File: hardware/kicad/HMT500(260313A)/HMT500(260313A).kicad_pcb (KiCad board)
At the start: 4 copper layers, 56.5 x 23 mm, 0 parts

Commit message: Rename project to HMT500(260313); circuit/PCB/Gerber files = HMT500(260313A)
- KiCad folder and all circuit files renamed to HMT500(260313A)*
  (top sheet, sub-sheets, symbol lib file, BOM, parts list, PDF, PCB);
  library nickname HMT500_260313A (no parentheses in lib_id)
- Title blocks carry Project No. HMT500(260313A); product HMT500(260313)
- PCB bottom silkscreen marking "HMT500(260313A)"
- export_gerbers.sh: Gerbers/drill named HMT500(260313A)-*, zip HMT500(260313A).zip
- Docs, mech drawing title block and references updated; decision #25
- Schematic review vs datasheets/KiCad library + optimization plan
  (docs/hw/schematic-review-260313A.md), awaiting approval

Co-Authored-By: Claude Opus 5.5 <noreply@anthropic.com>
Claude-Session: https://claude.ai/code/session_01JA2o8uJsqp9Vzsg4b665ev
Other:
- board text added: "HMT500(260313A)"
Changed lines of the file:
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@@
   (paper "A4")
   (title_block
-    (title "HMT500 PCB E-301 (outline & keepouts)")
+    (title "HMT500(260313A) PCB E-301 (outline & keepouts)")
     (date "2026-09-29")
     (rev "F")
@@
     (polygon (pts (xy 144.2 112.0) (xy 148.8 112.0) (xy 148.8 109.7) (xy 144.2 109.7)))
   )
-  (gr_rect (start 103.7 92.0) (end 119.3 108.0) (layer "Dwgs.User") (width 0.1) (fill none))
-  (gr_text "MEASUREMENT" (at 111.5 93.2) (layer "Dwgs.User")
+  (gr_rect (start 103.7 92.0) (end 120.3 108.0) (layer "Dwgs.User") (width 0.1) (fill none))
+  (gr_text "MEASUREMENT" (at 112.0 93.2) (layer "Dwgs.User")
     (effects (font (size 1.0 1.0) (thickness 0.150))))
-  (gr_text "J3, PCAP04, ADS1220, Cref" (at 111.5 106.8) (layer "Dwgs.User")
+  (gr_text "J3, PCAP04, ADS1220, Cref" (at 112.0 106.8) (layer "Dwgs.User")
     (effects (font (size 0.5 0.5) (thickness 0.075))))
-  (gr_rect (start 119.7 92.0) (end 135.3 108.0) (layer "Dwgs.User") (width 0.1) (fill none))
-  (gr_text "MCU + POWER" (at 127.5 93.2) (layer "Dwgs.User")
+  (gr_rect (start 120.7 92.0) (end 135.3 108.0) (layer "Dwgs.User") (width 0.1) (fill none))
+  (gr_text "MCU + POWER" (at 128.0 93.2) (layer "Dwgs.User")
     (effects (font (size 1.0 1.0) (thickness 0.150))))
-  (gr_text "STM32G0B1, eFuse, buck, LDO" (at 127.5 106.8) (layer "Dwgs.User")
+  (gr_text "STM32G0B1, eFuse, buck, LDO" (at 128.0 106.8) (layer "Dwgs.User")
     (effects (font (size 0.5 0.5) (thickness 0.075))))
   (gr_rect (start 135.7 92.0) (end 156.3 108.0) (layer "Dwgs.User") (width 0.1) (fill none))
@@
   (gr_text "J1, DAC8760x2, TPS26611, THVD2450" (at 146.0 106.8) (layer "Dwgs.User")
     (effects (font (size 0.5 0.5) (thickness 0.075))))
-  (gr_rect (start 108.0 96.5) (end 112.0 103.5) (layer "Dwgs.User") (width 0.1) (fill none))
-  (gr_text "J3 JST SH 4P SM04B-SRSS-TB (side entry <- front)" (at 110.0 104.3) (layer "Dwgs.User")
+  (gr_rect (start 116.0 96.5) (end 120.0 103.5) (layer "Dwgs.User") (width 0.1) (fill none))
+  (gr_text "J3 JST SH 4P SM04B-SRSS-TB (side entry <- front)" (at 118.0 104.3) (layer "Dwgs.User")
     (effects (font (size 0.5 0.5) (thickness 0.075))))
   (gr_rect (start 138.0 93.6) (end 144.0 106.4) (layer "Dwgs.User") (width 0.1) (fill none))
   (gr_text "J1 JST GH 8P SM08B-GHS-TB (side entry -> rear)" (at 141.0 107.2) (layer "Dwgs.User")
     (effects (font (size 0.5 0.5) (thickness 0.075))))
+  (gr_text "HMT500(260313A)" (at 44.5 0) (layer "B.SilkS")
+    (effects (font (size 1.2 1.2) (thickness 0.18)) (justify mirror)))
   (gr_text "Component height limit per side (incl. 0.5 margin):" (at 120.0 114.0) (layer "Cmts.User")
     (effects (font (size 0.8 0.8) (thickness 0.120))))

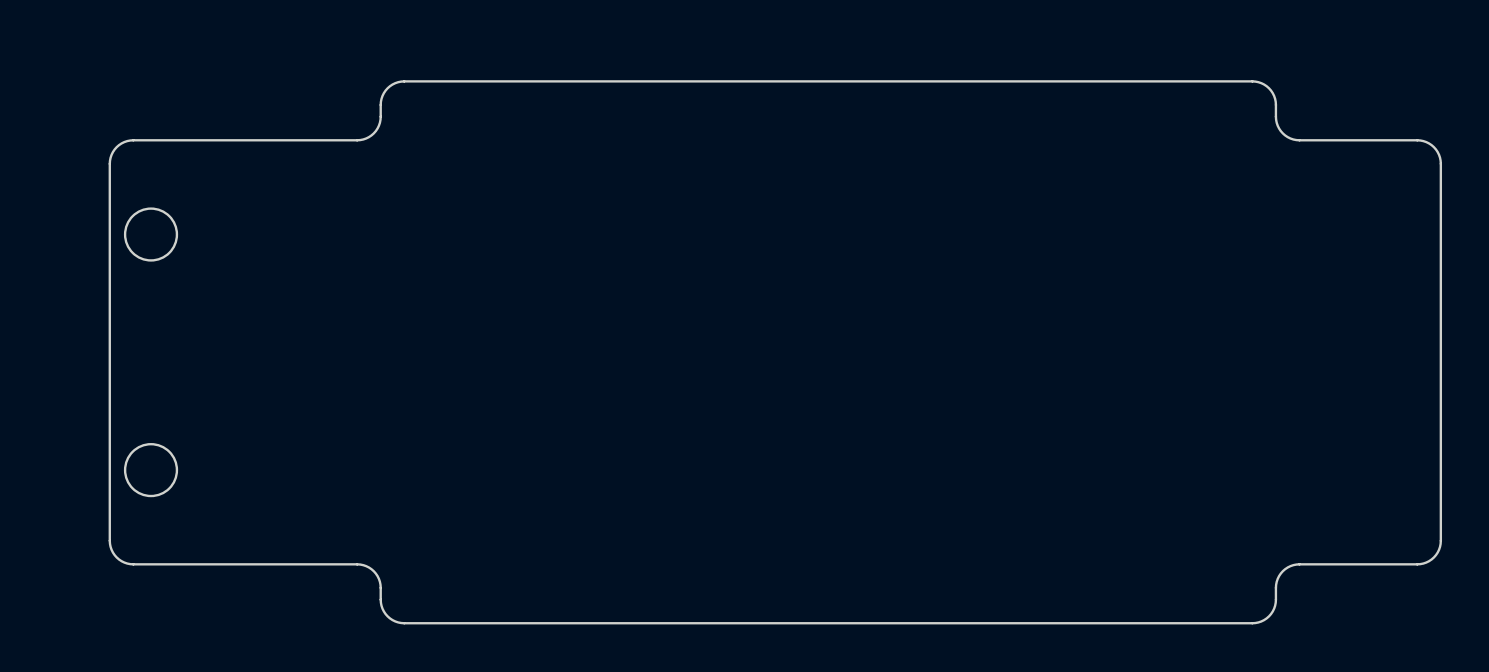
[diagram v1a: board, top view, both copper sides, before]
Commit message: PCB placement: all 84 parts placed and netted (before routing)
- place_pcb.py: fixed J3/J1/U4, hand slots for large parts, nearest-free
  search for passives; checks board edge and fillets, holder/ring keepouts,
  harness plug paths on top, height vs bore, courtyard overlap, holes
- plot_placement.py + placement.png/json (mech coords) for review and the
  assembly simulation
- Board rules for 4-layer: clearance/track 0.15, via 0.45/0.2, edge 0.3;
  .kicad_pro now merged (schematic sheet list kept)
- Custom footprints: fix local pad/line coordinates (pads were at 0,0);
  TVS3301 floating pad keeps number 9 (no symbol pin, no net)
- Placement tests; docs/hw/pcb-placement-260313A.md (J5 reach issue)

Co-Authored-By: Claude Opus 5.5 <noreply@anthropic.com>
Claude-Session: https://claude.ai/code/session_01JA2o8uJsqp9Vzsg4b665ev
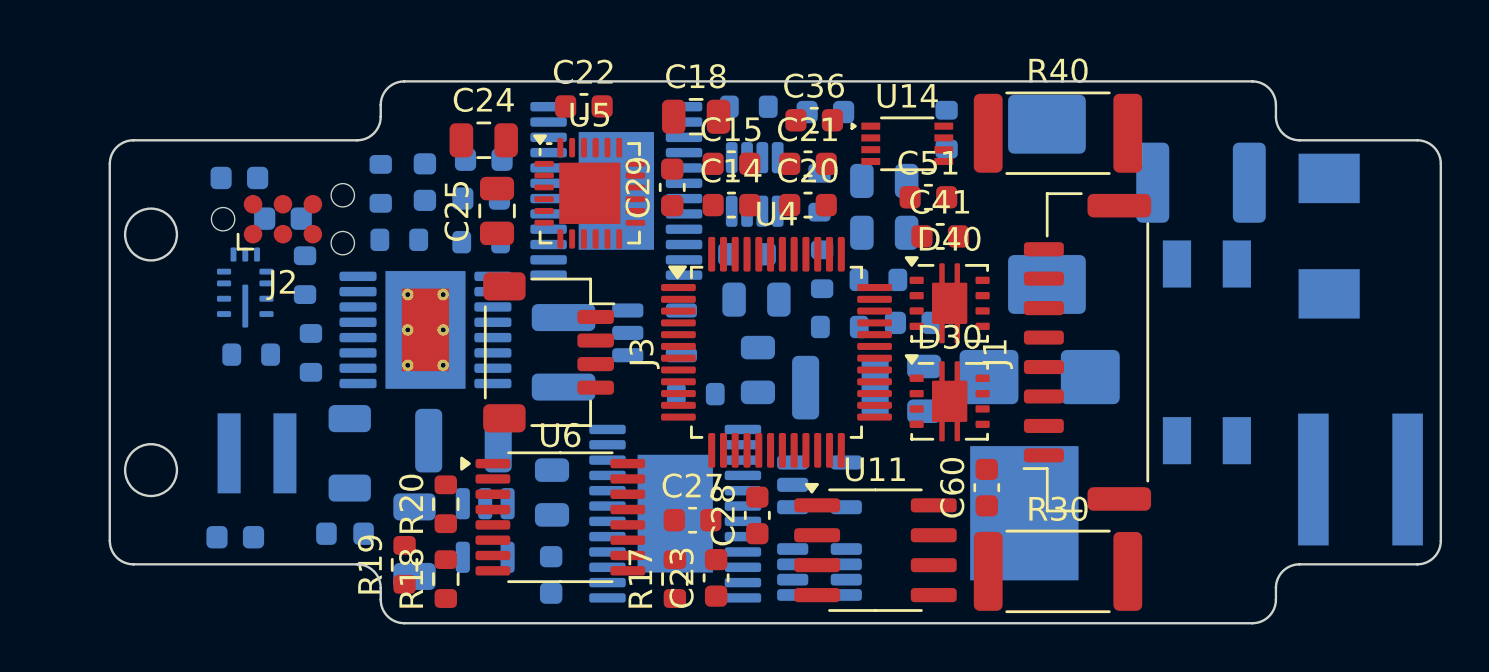
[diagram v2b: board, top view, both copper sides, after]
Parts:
- added C1: 100n 100V, Capacitor_SMD:C_0805_2012Metric, B.Cu at (134.6, 101.5)
- added C10: 22u 25V, Capacitor_SMD:C_1206_3216Metric, B.Cu at (110.2, 104.3)
- added C11: 20p C0G, Capacitor_SMD:C_0603_1608Metric, B.Cu at (105.3, 107.8)
- added C12: 1u, Capacitor_SMD:C_0603_1608Metric, B.Cu at (118.7, 109.5)
- added C13: 10u, Capacitor_SMD:C_0805_2012Metric, B.Cu at (118.8, 106.0)
- added C14: 100n, Capacitor_SMD:C_0603_1608Metric, F.Cu at (126.4, 93.8)
- added C15: 100n, Capacitor_SMD:C_0603_1608Metric, F.Cu at (126.4, 92.0)
- added C18: 4.7u, Capacitor_SMD:C_0805_2012Metric, F.Cu at (124.9, 90.0)
- added C20: 100n, Capacitor_SMD:C_0603_1608Metric, F.Cu at (129.6, 93.8)
- added C21: 100n, Capacitor_SMD:C_0603_1608Metric, F.Cu at (129.6, 92.0)
- added C22: 220p C0G 1%, Capacitor_SMD:C_0603_1608Metric, F.Cu at (120.1, 89.6)
- added C23: 100n, Capacitor_SMD:C_0603_1608Metric, F.Cu at (125.7, 109.6)
- added C24: 10u, Capacitor_SMD:C_0805_2012Metric, F.Cu at (115.9, 91.0)
- added C25: 4.7u, Capacitor_SMD:C_0805_2012Metric, F.Cu at (116.4, 94.0)
- added C27: 10n, Capacitor_SMD:C_0603_1608Metric, F.Cu at (124.7, 107.1)
- added C28: 100n, Capacitor_SMD:C_0603_1608Metric, F.Cu at (127.5, 106.9)
- added C29: 100n, Capacitor_SMD:C_0603_1608Metric, F.Cu at (123.9, 93.0)
- added C3: 4.7n 2kV Y2, Capacitor_SMD:C_1812_4532Metric, B.Cu at (146.3, 92.8)
- added C36: 100n, Capacitor_SMD:C_0603_1608Metric, F.Cu at (129.9, 90.2)
- added C4: 22n, Capacitor_SMD:C_0603_1608Metric, B.Cu at (115.8, 93.5)
- added C40: 100n, Capacitor_SMD:C_0603_1608Metric, B.Cu at (134.1, 98.8)
- added C41: 1n 100V, Capacitor_SMD:C_0603_1608Metric, F.Cu at (135.2, 95.1)
- added C42: 100n 50V, Capacitor_SMD:C_0805_2012Metric, B.Cu at (132.9, 94.9)
- added C43: 4.7u 50V, Capacitor_SMD:C_1210_3225Metric, B.Cu at (131.0, 101.5)
- added C44: 100n, Capacitor_SMD:C_0603_1608Metric, B.Cu at (113.4, 92.8)
- added C45: 100n 50V, Capacitor_SMD:C_0805_2012Metric, B.Cu at (127.5, 100.8)
- added C5: 10u 50V, Capacitor_SMD:C_1210_3225Metric, B.Cu at (119.3, 100.0)
- added C50: 100n, Capacitor_SMD:C_0603_1608Metric, B.Cu at (130.4, 89.8)
- added C51: 1n 100V, Capacitor_SMD:C_0603_1608Metric, F.Cu at (134.8, 93.4)
- added C52: 100n 50V, Capacitor_SMD:C_0805_2012Metric, B.Cu at (132.9, 92.7)
- added C54: 100n, Capacitor_SMD:C_0603_1608Metric, B.Cu at (115.9, 91.8)
- added C55: 100n 50V, Capacitor_SMD:C_0805_2012Metric, B.Cu at (127.5, 97.8)
- added C6: 22u 25V, Capacitor_SMD:C_1206_3216Metric, B.Cu at (112.9, 108.0)
- added C60: 100n, Capacitor_SMD:C_0603_1608Metric, F.Cu at (137.2, 105.7)
- added C7: 2.2u 100V, Capacitor_SMD:C_1210_3225Metric, B.Cu at (115.0, 103.8)
- added C8: 100n, Capacitor_SMD:C_0603_1608Metric, B.Cu at (107.3, 94.3)
- added C9: 1u, Capacitor_SMD:C_0603_1608Metric, B.Cu at (105.5, 92.6)
- added D1: SMDJ36CA, Diode_SMD:D_SMC, B.Cu at (139.8, 93.7)
- added D2: SMBJ33CA, Diode_SMD:D_SMB, B.Cu at (139.5, 101.0)
- added D30: TVS3301DRBR, HMT500_260313A:Texas_DRB0008A_PadFloat, F.Cu at (135.7, 102.1)
- added D40: TVS3301DRBR, HMT500_260313A:Texas_DRB0008A_PadFloat, F.Cu at (135.7, 97.9)
- added FB1: 600R@100MHz, Inductor_SMD:L_0603_1608Metric, B.Cu at (110.0, 107.7)
- added GDT1: 2035-23-SM, HMT500_260313A:GDT_Bourns_2035-xx-SM, B.Cu at (153.1, 105.4)
- added J1: SM08B-GHS-TB, Connector_JST:JST_GH_SM08B-GHS-TB_1x08-1MP_P1.25mm_Horizontal, F.Cu at (141.5, 100.0)
- added J2: TC2030-IDC-NL, Connector:Tag-Connect_TC2030-IDC-NL_2x03_P1.27mm_Vertical, F.Cu at (107.3, 94.3)
- added J3: SM04B-SRSS-TB, Connector_JST:JST_SH_SM04B-SRSS-TB_1x04-1MP_P1.00mm_Horizontal, F.Cu at (118.6, 100.0)
- added J5: S1941-46R, Connector:SpringContact_Harwin_S1941-46R, B.Cu at (139.9, 106.8)
- added L1: CMC 1mH 0.8A, Inductor_SMD:L_CommonMode_Wuerth_WE-SL2, B.Cu at (146.6, 100.0)
- added L2: 15uH, Inductor_SMD:L_Coilcraft_XAL4030-XXX, B.Cu at (106.2, 104.3)
- added R1: 4.7R 1W pulse, Resistor_SMD:R_MELF_MMB-0207, B.Cu at (151.8, 95.1)
- added R17: 1k, Resistor_SMD:R_0603_1608Metric, F.Cu at (124.0, 109.6)
- added R18: 1k, Resistor_SMD:R_0603_1608Metric, F.Cu at (114.3, 109.6)
- added R19: 4.02k 0.02% 5ppm, Resistor_SMD:R_0603_1608Metric, F.Cu at (112.5, 109.0)
- added R2: 1M, Resistor_SMD:R_0603_1608Metric, B.Cu at (135.5, 90.5)
- added R20: 1k, Resistor_SMD:R_0603_1608Metric, F.Cu at (114.3, 106.5)
- added R3: 866k 1%, Resistor_SMD:R_0603_1608Metric, B.Cu at (108.5, 100.0)
- added R30: 10R pulse, Resistor_SMD:R_2512_6332Metric, F.Cu at (140.2, 109.3)
- added R31: 10k, Resistor_SMD:R_0603_1608Metric, B.Cu at (131.0, 98.9)
- added R32: 15k 0.1% 25ppm, Resistor_SMD:R_0603_1608Metric, B.Cu at (124.9, 101.8)
- added R33: 10k, Resistor_SMD:R_0603_1608Metric, B.Cu at (127.0, 95.8)
- added R34: 10R, Resistor_SMD:R_0603_1608Metric, B.Cu at (132.6, 96.9)
- added R4: 97.6k 1%, Resistor_SMD:R_0603_1608Metric, B.Cu at (108.3, 96.7)
- added R40: 10R pulse, Resistor_SMD:R_2512_6332Metric, F.Cu at (140.2, 90.7)
- added R41: 10k, Resistor_SMD:R_0603_1608Metric, B.Cu at (130.2, 96.5)
- added R42: 15k 0.1% 25ppm, Resistor_SMD:R_0603_1608Metric, B.Cu at (127.1, 89.6)
- added R44: 10R, Resistor_SMD:R_0603_1608Metric, B.Cu at (130.1, 93.2)
- added R5: 41.2k 1%, Resistor_SMD:R_0603_1608Metric, B.Cu at (112.3, 95.2)
- added R6: 80.6k 1%, Resistor_SMD:R_0603_1608Metric, B.Cu at (115.8, 95.3)
- added R8: 100k 1%, Resistor_SMD:R_0603_1608Metric, B.Cu at (106.0, 100.1)
- added R9: 24.9k 1%, Resistor_SMD:R_0603_1608Metric, B.Cu at (111.5, 92.8)
- added U1: TPS26600PWPR, Package_SO:HTSSOP-16-1EP_4.4x5mm_P0.65mm_EP3.4x5mm_Mask2.46x2.31mm_ThermalVias, B.Cu at (113.4, 99.0)
- added U10: TPS26611DDFR, Package_TO_SOT_SMD:SOT-23-8, B.Cu at (127.4, 92.9)
- added U11: THVD2450DR, Package_SO:SOIC-8_3.9x4.9mm_P1.27mm, F.Cu at (132.5, 108.4)
- added U12: OPA197IDBVR, Package_TO_SOT_SMD:SOT-23-5, B.Cu at (130.1, 105.6)
- added U13: OPA197IDBVR, Package_TO_SOT_SMD:SOT-23-5, B.Cu at (123.1, 99.2)
- added U14: SN74LVC2G32DCUR, Package_SO:VSSOP-8_2.3x2mm_P0.5mm, F.Cu at (133.8, 91.2)
- added U2: LMR36006BRNXR, HMT500_260313A:Texas_RNX0012A_VQFN-HR-12_2x3mm, B.Cu at (105.8, 97.2)
- added U3: TPS7A2033PDBVR, Package_TO_SOT_SMD:SOT-23-5, B.Cu at (115.9, 107.6)
- added U4: STM32G0B1CCT3, Package_QFP:LQFP-48_7x7mm_P0.5mm, F.Cu at (128.3, 100.0)
- added U5: PCAP04-AQFM-24, Package_DFN_QFN:QFN-24-1EP_4x4mm_P0.5mm_EP2.6x2.6mm, F.Cu at (120.4, 93.2)
- added U6: ADS1220IPWR, Package_SO:TSSOP-16_4.4x5mm_P0.65mm, F.Cu at (119.1, 107.0)
- added U7: DAC8760IPWP, Package_SO:HTSSOP-24-1EP_4.4x7.8mm_P0.65mm_EP3.2x5mm, B.Cu at (124.0, 106.8)
- added U8: DAC8760IPWP, Package_SO:HTSSOP-24-1EP_4.4x7.8mm_P0.65mm_EP3.2x5mm, B.Cu at (121.5, 93.2)
- added U9: TPS26611DDFR, Package_TO_SOT_SMD:SOT-23-8, B.Cu at (130.1, 109.3)

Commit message: PCB placement rev 2: relax harness paths, use the freed top area
- Top harness paths: only plug body + insertion/grip space kept empty;
  under W-1 wires (z 2.2) and W-2 wires parts up to 1.0 mm allowed;
  last 2 mm before the M12 end kept empty (wires drop over the edge)
- J2 Tag-Connect (flat) moved under the W-1 wires; LDO U3, FB1, C12, C13
  moved to the freed top front area (+3V3A right at the measurement)
- eFuse U1 under the J3 plug path (its thermal-via top pad needs a
  part-free top); buck loop U2-L2-C10/C6 tightened; U14 next to MCU
- Bands stored in placement.json; plot and tests read them

Co-Authored-By: Claude Opus 5.5 <noreply@anthropic.com>
Claude-Session: https://claude.ai/code/session_01JA2o8uJsqp9Vzsg4b665ev
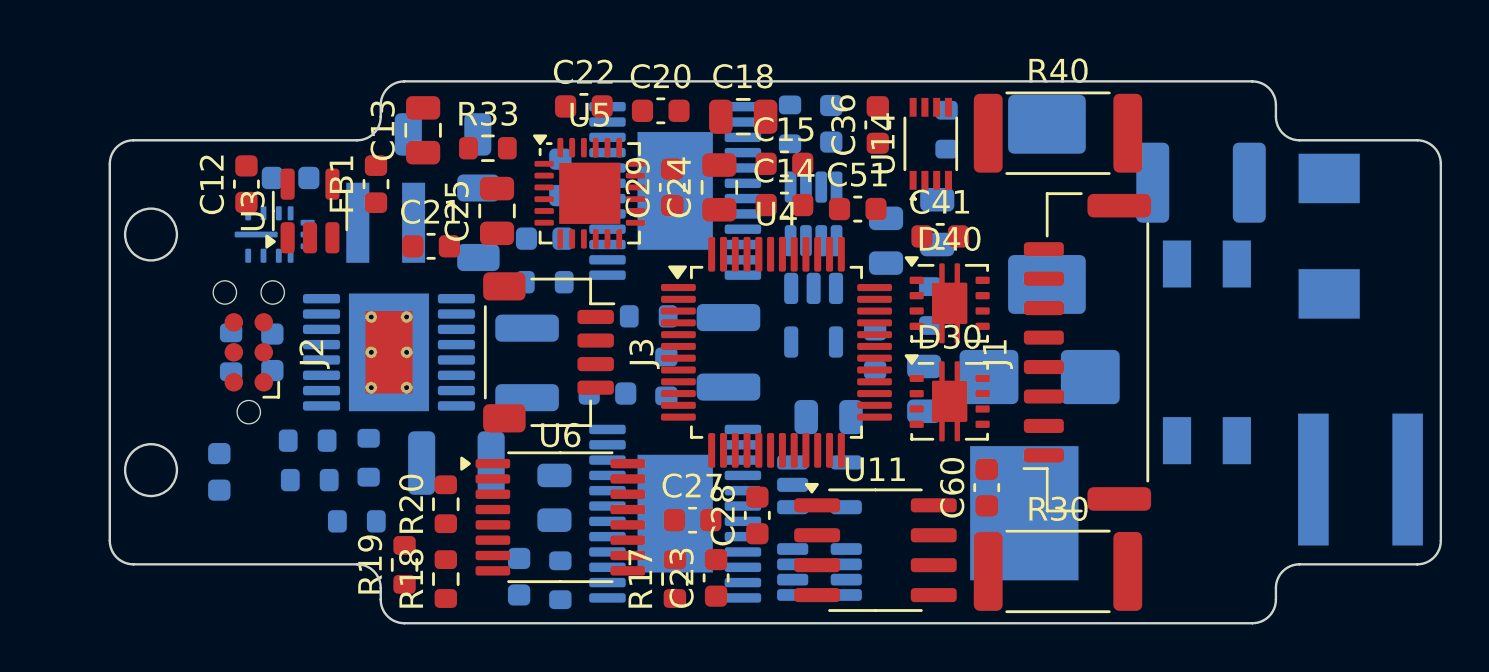
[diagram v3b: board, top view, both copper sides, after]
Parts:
- C12, C13, FB1, R33, U3: moved to F.Cu
- moved C12 21.0 mm to (105.8, 92.9), turned to 90 degrees
- moved R34 18.6 mm to (119.1, 109.7), turned to -90 degrees
- moved C42 18.0 mm to (118.9, 106.2), turned to -90 degrees
- moved C6 17.3 mm to (114.1, 90.8), turned to 0 degrees
- moved C44 17.2 mm to (117.4, 109.5)
- moved C21 16.4 mm to (113.6, 95.5)
- moved C13 16.3 mm to (113.3, 90.6), turned to 90 degrees
- moved U3 15.5 mm to (108.5, 94.0), turned to 90 degrees
- moved FB1 14.9 mm to (111.3, 92.9), turned to 90 degrees
- moved C40 13.3 mm to (121.1, 101.8)
- moved R5 12.1 mm to (110.5, 107.2)
- moved R33 11.9 mm to (116.0, 91.3)
- moved R9 11.3 mm to (108.4, 103.8), turned to 0 degrees
- moved L2 11.2 mm to (111.7, 94.5)
- moved C10 11.2 mm to (115.6, 94.5)
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
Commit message: Apply assembly-simulation fixes A-F; re-simulation NG 0
- A: holder M-105 window 5.6 x 3.2 above the PCB slot (W-1 plug passes
  with the PCB already fitted); bench sub-assembly for the cross screws
- B: PCB wide section ends at x 63.4 (0.6 mm to the endcap face)
- C: placement height rule behind the ring (x >= 59) uses Ø20
- D: J5 spring contact removed; J5 = solder hole for a chassis wire to an
  M2 ring terminal under the holder top screw (M2x8, cbore Ø5.2 x 2.2);
  C3/R2 moved next to J5 (GDT1 mid-board, route CHASSIS wide)
- E: W-2 harness 60 -> 40 mm; top area behind J1 kept part-free
- F: assembly tool T-001 push bar (STEP for 3D printing)
- CAD reads the real PCB placement; drawings Rev G with the new sequence;
  simulation rewritten for the new sequence (23 checks, NG 0)
- Decision #27; docs updated

Co-Authored-By: Claude Opus 5.5 <noreply@anthropic.com>
Claude-Session: https://claude.ai/code/session_01JA2o8uJsqp9Vzsg4b665ev
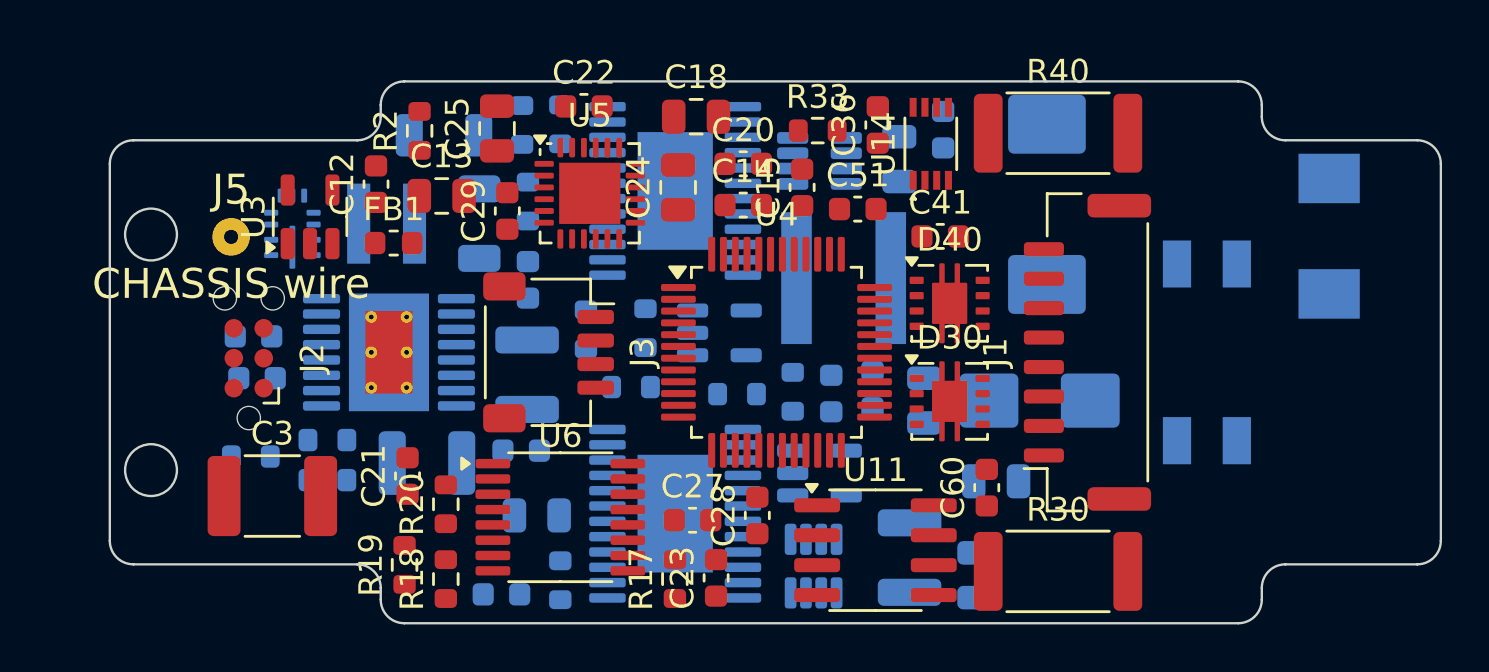
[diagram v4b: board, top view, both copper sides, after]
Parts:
- C3, R2: moved to F.Cu
- J5: value S1941-46R -> CHASSIS wire; footprint Connector:SpringContact_Harwin_S1941-46R -> HMT500_260313A:SolderWire_Chassis_D0.6mm; moved to F.Cu
- moved C3 41.6 mm to (106.9, 106.1)
- moved J5 36.7 mm to (105.2, 95.1)
- moved GDT1 23.5 mm to (131.2, 96.8)
- moved R2 22.4 mm to (113.2, 90.6), turned to 90 degrees
- moved C54 16.0 mm to (132.4, 101.6)
- moved R8 15.7 mm to (117.5, 90.3)
- moved C11 15.4 mm to (117.8, 96.9)
- moved R33 14.0 mm to (130.1, 90.6)
- moved R9 13.8 mm to (117.8, 93.6), turned to -90 degrees
- moved R41 12.1 mm to (122.7, 99.0)
- moved C43 11.6 mm to (133.9, 108.7)
- moved C52 11.3 mm to (137.6, 105.5), turned to 0 degrees
- moved C21 9.80 mm to (112.6, 105.2), turned to 90 degrees
- moved R42 9.75 mm to (119.1, 90.3)
- moved C40 9.50 mm to (130.6, 101.8), turned to -90 degrees
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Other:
- outline, holes or cut-outs redrawn
- board text added: "11.5-48.9 mm: width 23, bore 27 -> edge 5.8 / center 12.2 mm"
- board text added: "48.9-56.5 mm: width 18, bore 22 -> edge 5.0 / center 9.7 mm"
- board text removed: "11.5-49.5 mm: width 23, bore 27 -> edge 5.8 / center 12.2 mm"
- board text removed: "49.5-56.5 mm: width 18, bore 22 -> edge 5.0 / center 9.7 mm"
